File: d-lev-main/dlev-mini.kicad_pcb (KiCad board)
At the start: 4 copper layers, 175.3 x 163.3 mm, 126 parts, among them J1 S12B-PH-SM4-TB, J2 Tag-Connect TC2030-NL, J3 S8B-PH-SM4-TB, J4 S8B-PH-SM4-TB, J5 S6B-PH-SM4-TB, Q1 BSS138, Q2 BSS138, Q3 BSS138, Q4 BSS138, Q5 BSS138, SW1 RotaryEncoder_Switch, SW2 RotaryEncoder_Switch, SW3 RotaryEncoder_Switch, SW4 RotaryEncoder_Switch, SW5 RotaryEncoder_Switch, SW6 RotaryEncoder_Switch, SW7 RotaryEncoder_Switch, SW8 RotaryEncoder_Switch, U1 25LCxxx, U3 AC608, U4 AMS1117-3.3

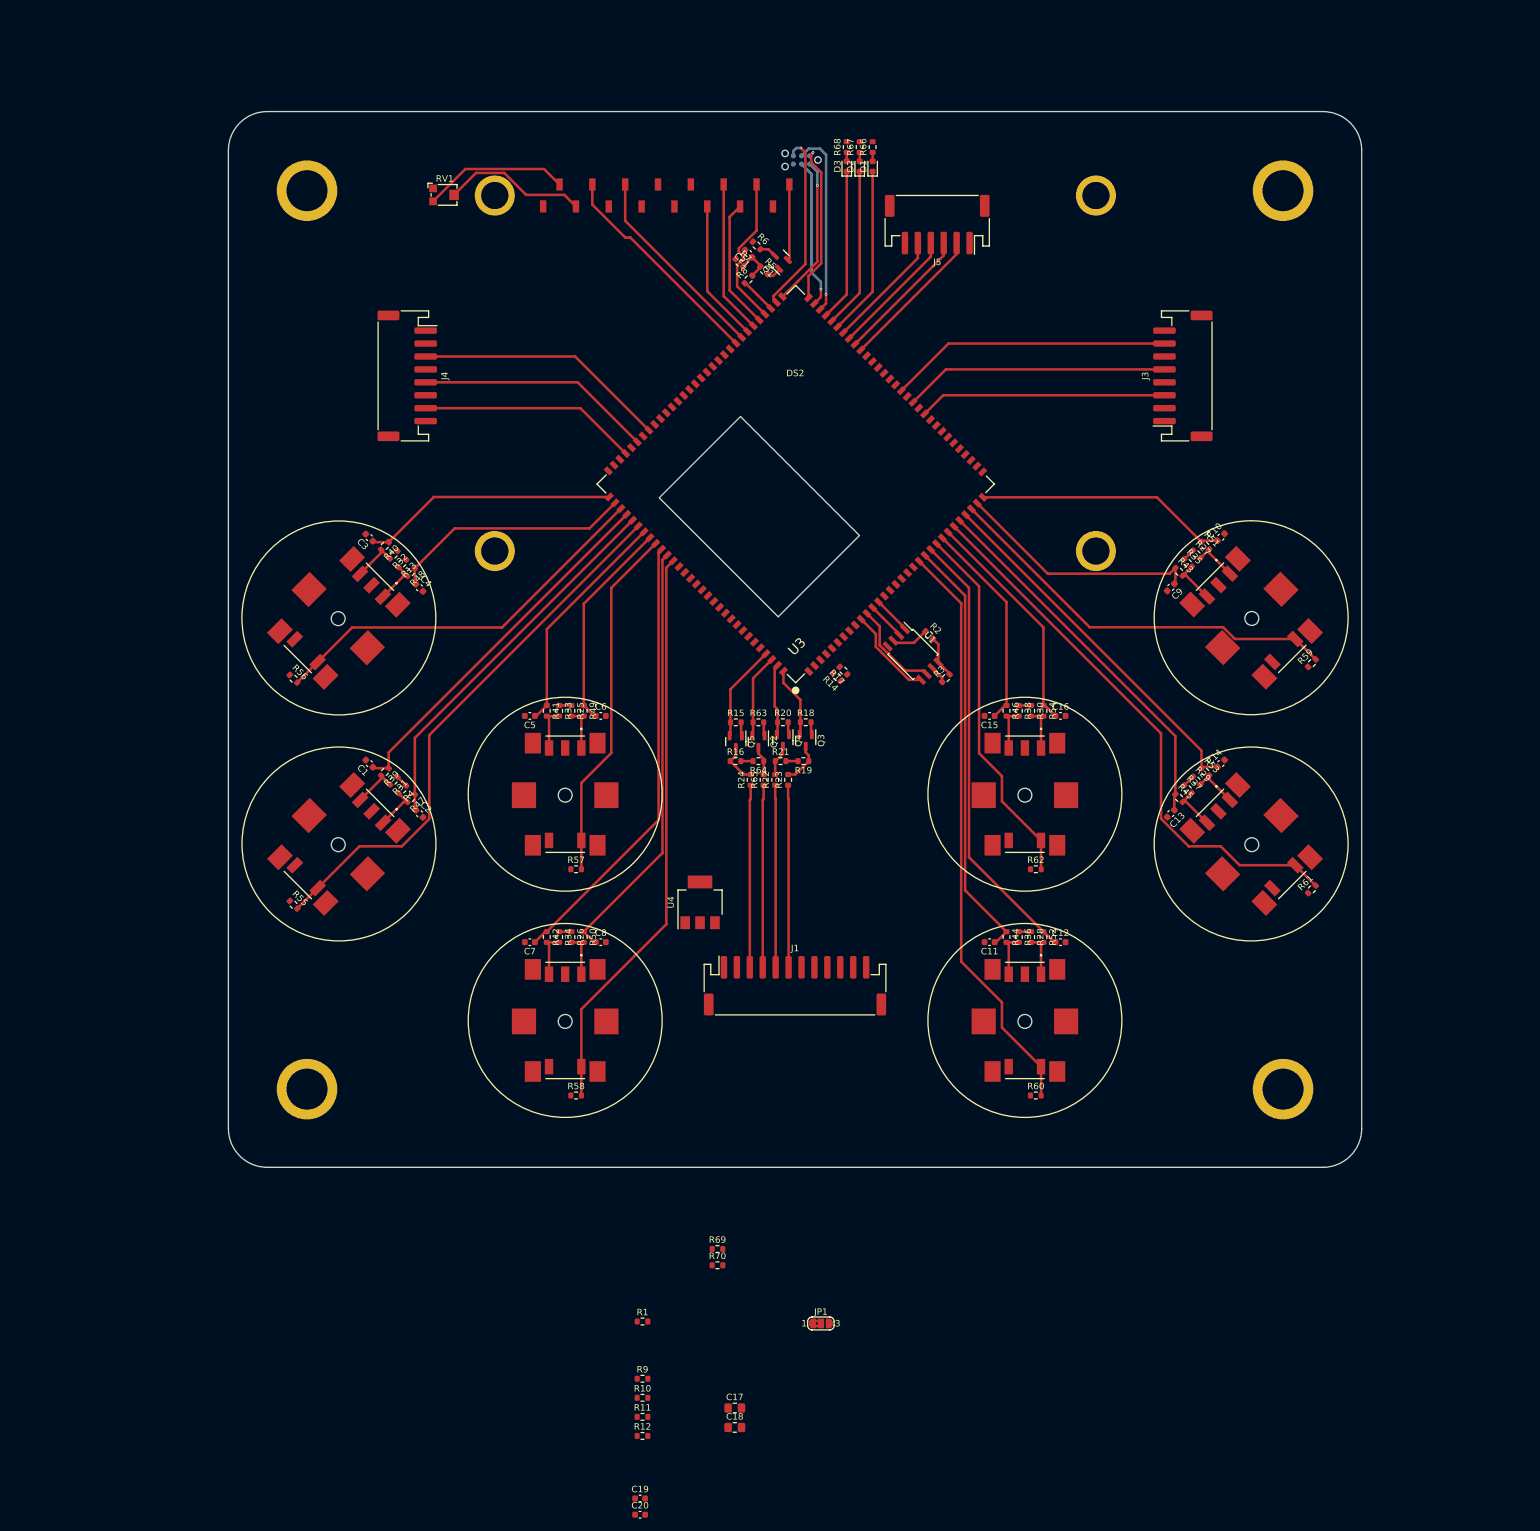
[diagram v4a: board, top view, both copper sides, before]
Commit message: four layer routes
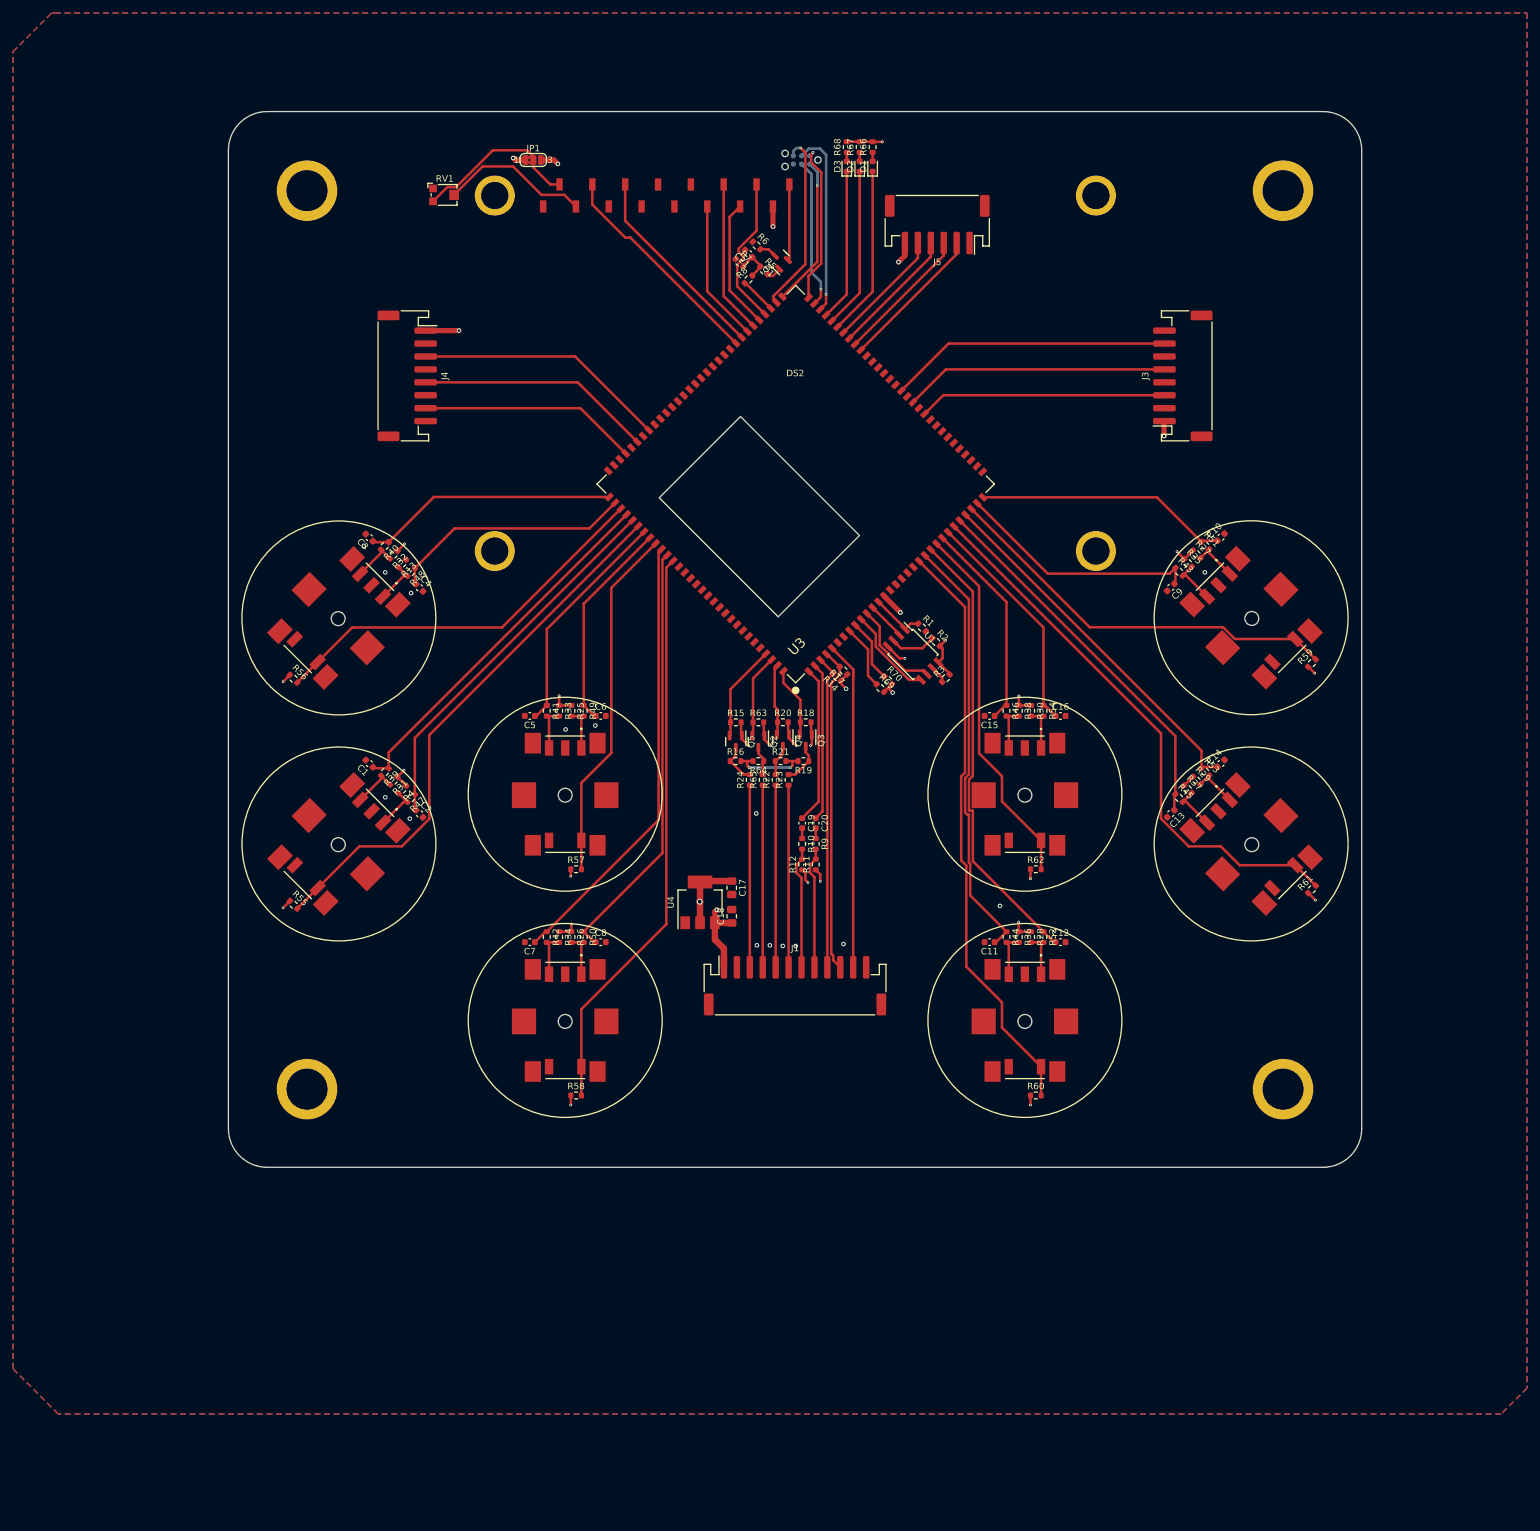
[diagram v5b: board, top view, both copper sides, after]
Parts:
- moved JP1 185.4 mm to (-40.5, -103.0)
- moved R1 115.7 mm to (19.6, -30.7), turned to -45 degrees
- moved C20 110.4 mm to (3.20, -0.40), turned to -90 degrees
- moved C19 107.4 mm to (1.10, -0.40), turned to -90 degrees
- moved R70 94.3 mm to (14.4, -22.5), turned to -45 degrees
- moved R12 91.8 mm to (1.10, 6.00), turned to 90 degrees
- moved R69 90.4 mm to (13.2, -21.3), turned to -45 degrees
- moved R11 89.6 mm to (3.20, 6.00), turned to 90 degrees
- moved R10 89.2 mm to (1.10, 2.80), turned to -90 degrees
- moved R9 87.0 mm to (3.20, 2.80), turned to -90 degrees
- moved C17 80.5 mm to (-9.80, 9.60), turned to -90 degrees
- moved C18 79.1 mm to (-9.80, 14.0), turned to 90 degrees
- moved R2 1.52 mm to (21.8, -28.4)
- moved R24 0.13 mm to (-7.00, -7.10)
- moved R65 0.13 mm to (-5.00, -7.10)
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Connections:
- C19 pad 1: /spdif_tx_1 -> /spdif_tx_0
- C20 pad 1: /spdif_tx_0 -> /spdif_tx_1
- DS2 pad 2: +5V -> /LCD/VLCD
- JP1 pad 2: +5V -> /LCD/VLCD
- RV1 pad 3: +5V -> /LCD/VLCD
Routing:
- net +5V: track 26.4 -> 297.9 mm, vias 0 -> 8
- net +3V3: track 28.0 -> 95.2 mm, vias 0 -> 26
- net mute_led: track 0.00 -> 50.7 mm
- net mute_btn: track 0.00 -> 50.5 mm
- net acal_btn: track 0.00 -> 48.8 mm
- net /LCD/VLCD: track 0.00 -> 26.0 mm
- net /spdif_tx_1: track 0.00 -> 24.5 mm
- net /spdif_tx_0: track 0.00 -> 24.4 mm
- net spdif_line: track 0.00 -> 19.0 mm
- net spdif_mon: track 0.00 -> 18.9 mm
- net /FPGA/gpio_i3: track 0.00 -> 10.0 mm
- net /FPGA/gpio_i2: track 0.00 -> 9.83 mm
- net GND: track 0.00 -> 7.85 mm, vias 0 -> 18
- net /FPGA/mem_spi.cs: track 5.92 -> 8.29 mm
- net Net-(C19-Pad2): track 0.00 -> 1.60 mm
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- added copper zone on In2.Cu, net +3V3
- added copper zone on B.Cu, net GND
- added copper zone on F.Cu, net GND
- added copper zone on In1.Cu, net GND

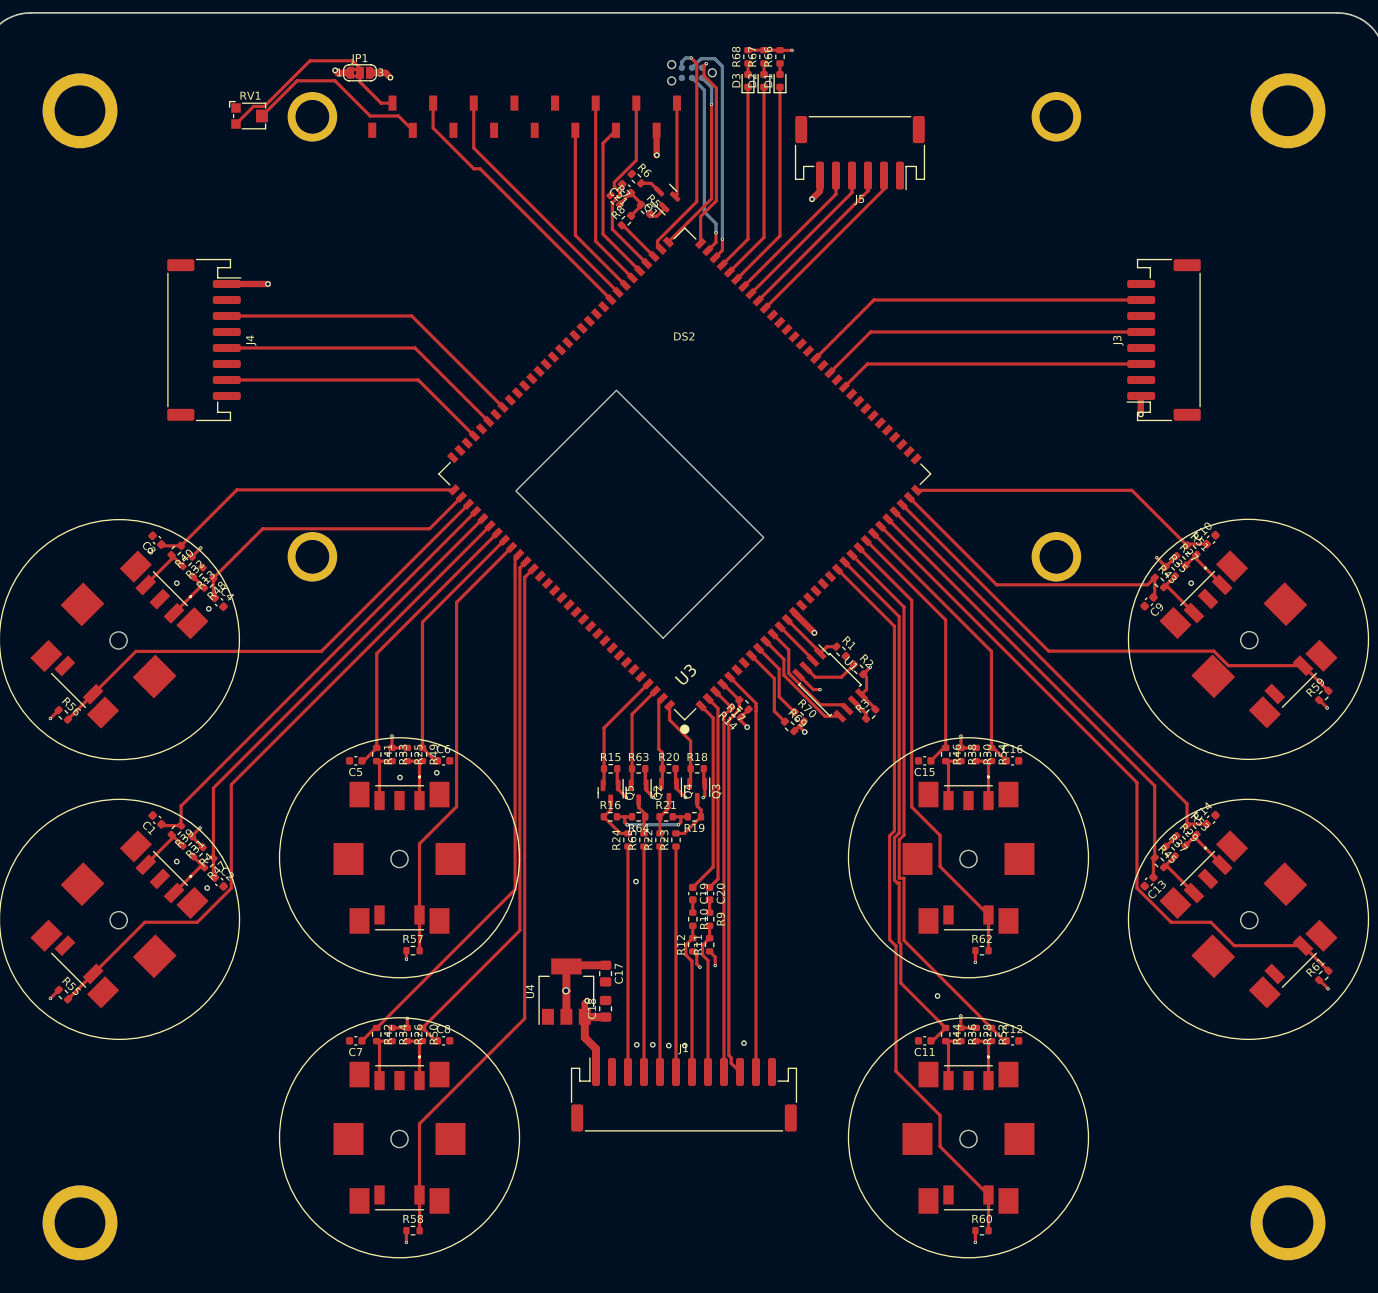
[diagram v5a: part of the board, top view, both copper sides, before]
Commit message: Clean up unroutes and add DRC
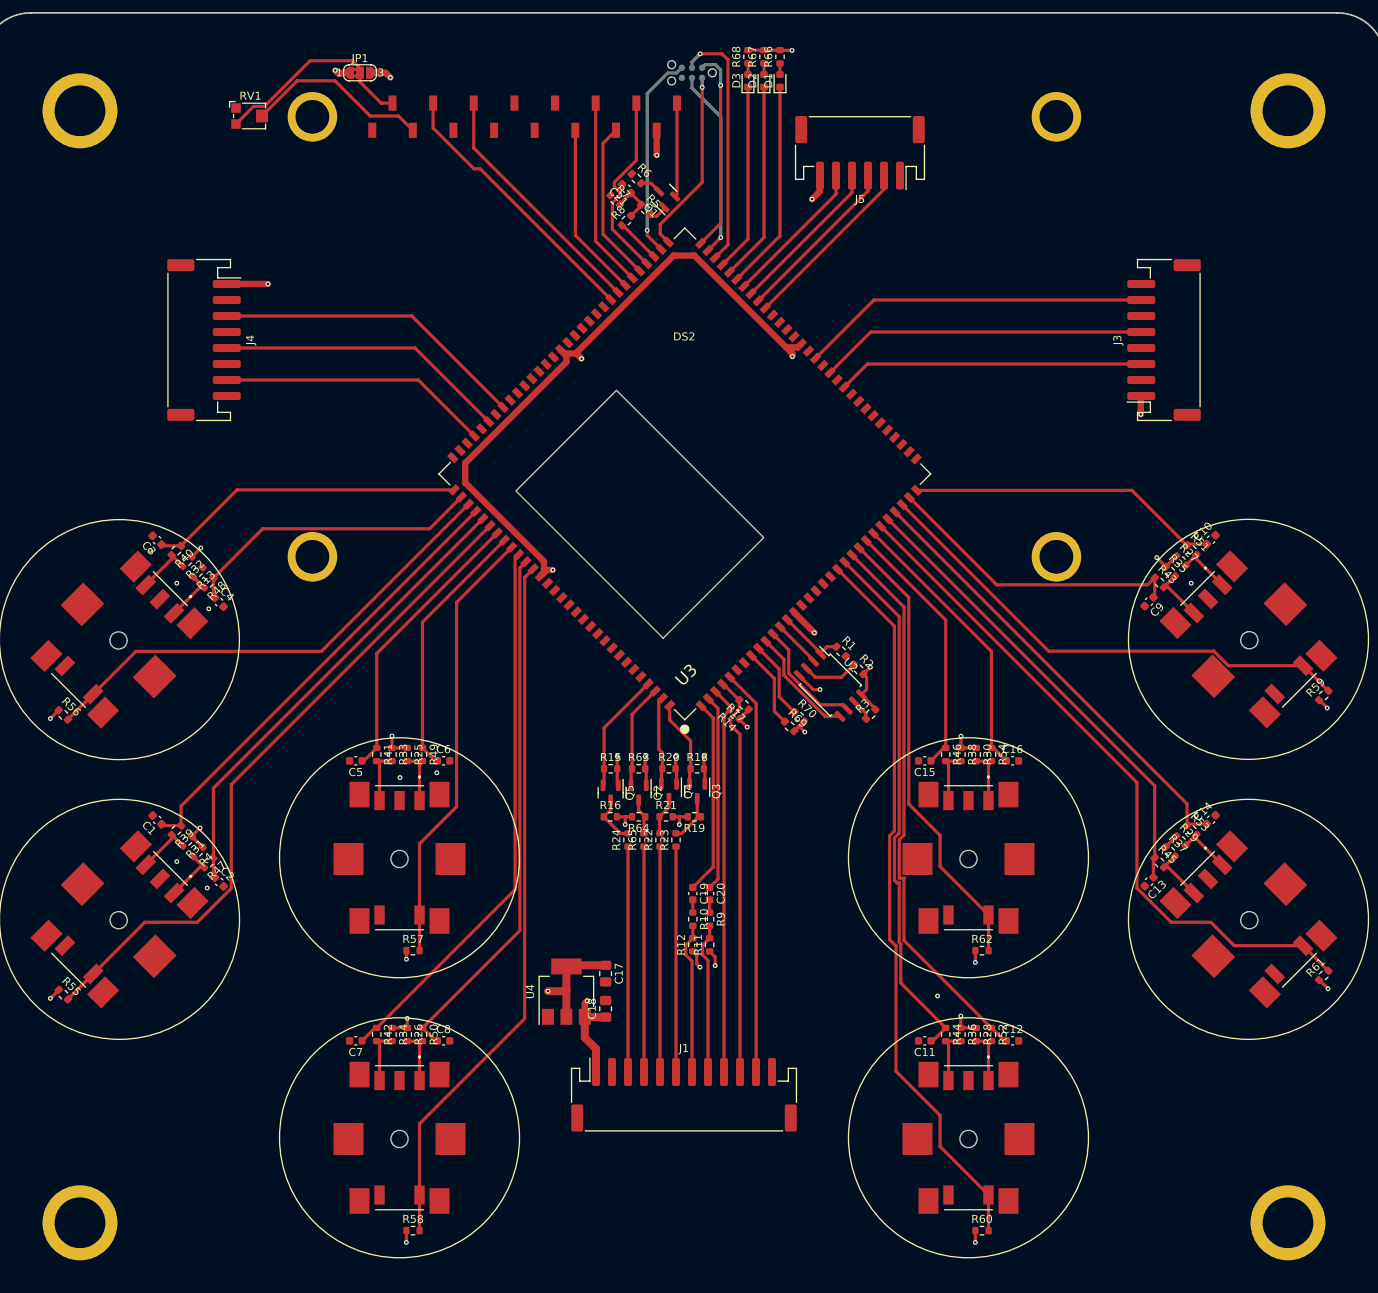
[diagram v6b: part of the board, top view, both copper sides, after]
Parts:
- removed U1: 25LCxxx, Package_SO:SOIC-8W_5.3x5.3mm_P1.27mm
- added U2: 25LCxxx, Package_SO:SOIC-8_5.275x5.275mm_P1.27mm, F.Cu at (18.3, -26.4)
- moved R14 0.21 mm to (6.37, -22.8)
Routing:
- net +3V3: track 95.2 -> 168.9 mm, vias 26 -> 29
- net /FPGA/TDO: track 28.5 -> 25.8 mm
- net /FPGA/TCK: track 29.0 -> 31.4 mm
- net +5V: track 297.9 -> 297.0 mm
- net /FPGA/TMS: track 24.8 -> 25.5 mm
- net GND: vias 18 -> 12
